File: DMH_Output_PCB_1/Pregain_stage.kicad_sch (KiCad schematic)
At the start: 9 parts, among them U7 TL072

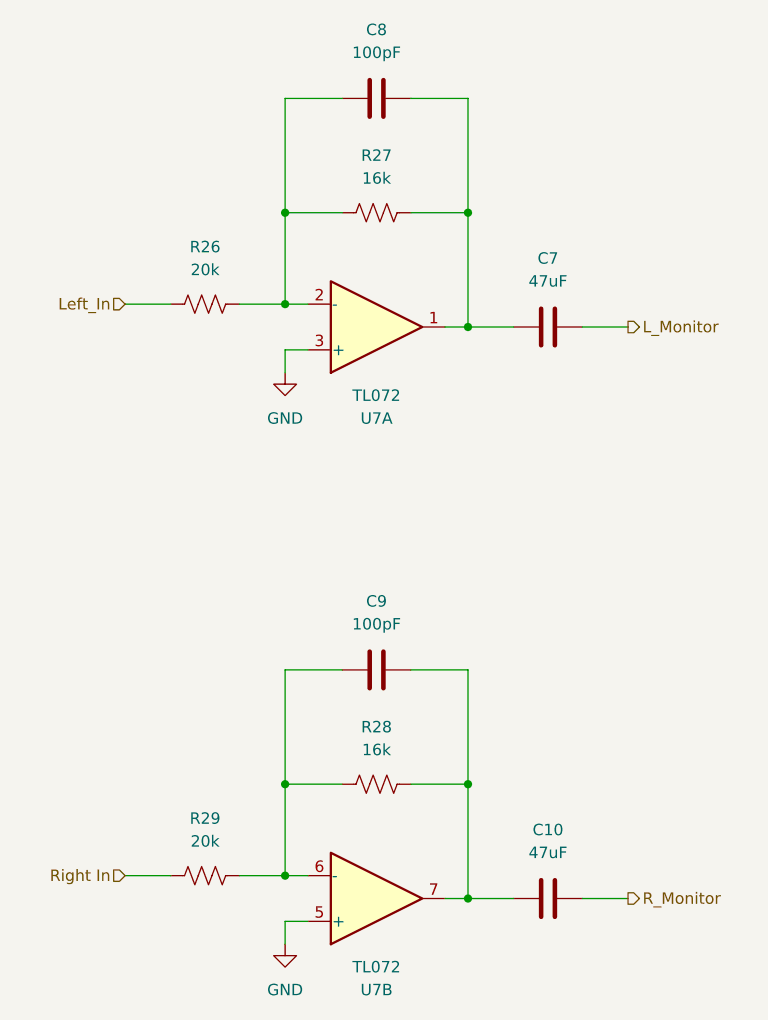
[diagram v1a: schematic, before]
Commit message: Redesigned external input preamp
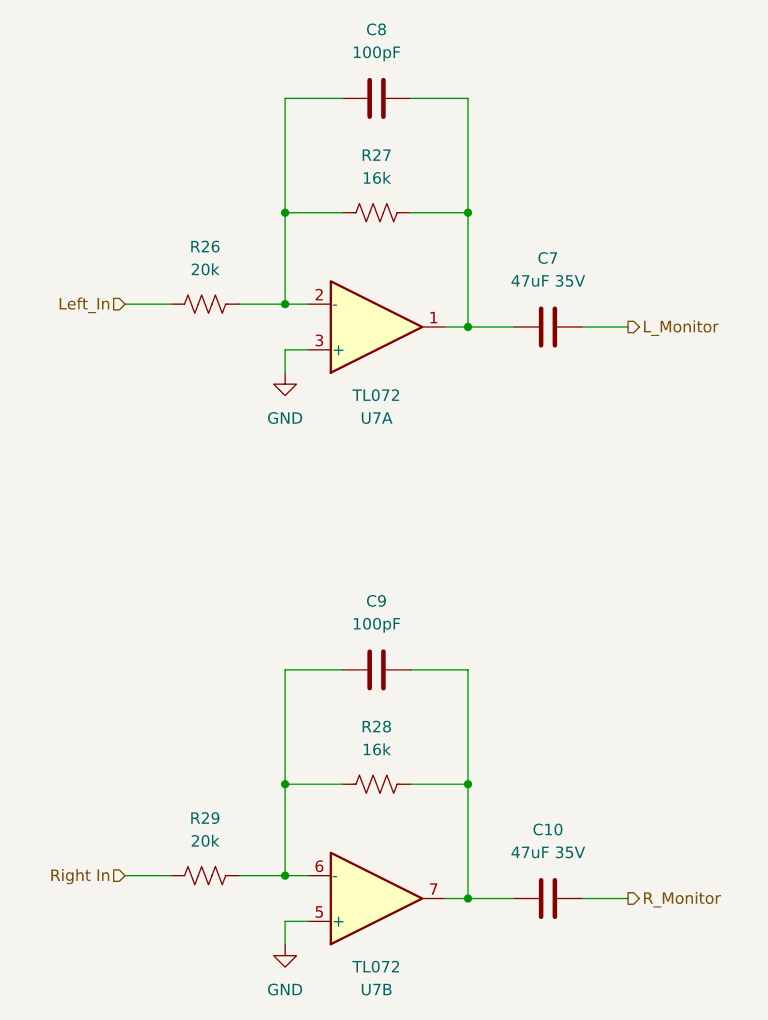
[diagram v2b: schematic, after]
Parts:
- C10, C7: value 47uF -> 47uF 35V; footprint Capacitor_THT:C_Disc_D4.3mm_W1.9mm_P5.00mm -> Capacitor_THT:C_Radial_D8.0mm_H11.5mm_P3.50mm
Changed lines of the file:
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@@
+	)
+	(symbol
+		(lib_id "Device:C")
+		(at 107.95 63.5 90)
+		(unit 1)
+		(exclude_from_sim no)
+		(in_bom yes)
+		(on_board yes)
+		(dnp no)
+		(fields_autoplaced yes)
+		(property "Reference" "C7"
+			(at 107.95 55.88 90)
+			(effects
+				(font
+					(size 1.27 1.27)
+				)
+			)
+		)
+		(property "Value" "47uF 35V"
+			(at 107.95 58.42 90)
+			(effects
+				(font
+					(size 1.27 1.27)
+				)
+			)
+		)
+		(property "Footprint" "Capacitor_THT:C_Radial_D8.0mm_H11.5mm_P3.50mm"
+			(at 111.76 62.5348 0)
+			(effects
+				(font
+					(size 1.27 1.27)
+				)
+				(hide yes)
+			)
+		)
+		(property "Datasheet" "~"
+			(at 107.95 63.5 0)
+			(effects
+				(font
+					(size 1.27 1.27)
+				)
+				(hide yes)
+			)
+		)
+		(property "Description" "Unpolarized capacitor"
+			(at 107.95 63.5 0)
+			(effects
+				(font
+					(size 1.27 1.27)
+				)
+				(hide yes)
+			)
+		)
+		(property "Function" ""
+			(at 107.95 63.5 0)
+			(effects
+				(font
+					(size 1.27 1.27)
+				)
+			)
+		)
+		(pin "1"
+		)
+		(pin "2"
+		)
+		(instances
+			(project "DMH_Output_PCB_1"
+				(path "/58f4306d-5387-4983-bb08-41a2313fd315/0b1658b3-ac7b-4692-8043-3e4b42d6c671"
+					(reference "C7")
+					(unit 1)
+				)
+			)
+		)
 	)
 	(symbol
@@
 	(symbol
 		(lib_id "Device:C")
-		(at 107.95 63.5 90)
-		(unit 1)
-		(exclude_from_sim no)
-		(in_bom yes)
-		(on_board yes)
-		(dnp no)
-		(fields_autoplaced yes)
-		(property "Reference" "C7"
-			(at 107.95 55.88 90)
-			(effects
-				(font
-					(size 1.27 1.27)
-				)
-			)
-		)
-		(property "Value" "47uF"
-			(at 107.95 58.42 90)
-			(effects
-				(font
-					(size 1.27 1.27)
-				)
-			)
-		)
-		(property "Footprint" "Capacitor_THT:C_Disc_D4.3mm_W1.9mm_P5.00mm"
-			(at 111.76 62.5348 0)
-			(effects
-				(font
-					(size 1.27 1.27)
-				)
-				(hide yes)
-			)
-		)
-		(property "Datasheet" "~"
-			(at 107.95 63.5 0)
-			(effects
-				(font
-					(size 1.27 1.27)
-				)
-				(hide yes)
-			)
-		)
-		(property "Description" "Unpolarized capacitor"
-			(at 107.95 63.5 0)
-			(effects
-				(font
-					(size 1.27 1.27)
-				)
-				(hide yes)
-			)
-		)
-		(pin "2"
-		)
-		(pin "1"
-		)
-		(instances
-			(project "DMH_Output_PCB_1"
-				(path "/58f4306d-5387-4983-bb08-41a2313fd315/0b1658b3-ac7b-4692-8043-3e4b42d6c671"
-					(reference "C7")
-					(unit 1)
-				)
-			)
-		)
-	)
-	(symbol
-		(lib_id "Device:C")
 		(at 107.95 127 90)
 		(unit 1)
@@
 			)
 		)
-		(property "Value" "47uF"
+		(property "Value" "47uF 35V"
 			(at 107.95 121.92 90)
 			(effects
@@
 			)
 		)
-		(property "Footprint" "Capacitor_THT:C_Disc_D4.3mm_W1.9mm_P5.00mm"
+		(property "Footprint" "Capacitor_THT:C_Radial_D8.0mm_H11.5mm_P3.50mm"
 			(at 111.76 126.0348 0)
 			(effects
@@
 			)
 		)
-		(pin "2"
-		)
-		(pin "1"
-		)
-		(instances
+		(property "Function" ""
+			(at 107.95 127 0)
+			(effects
+				(font
+					(size 1.27 1.27)
+				)
+			)
+		)
+		(pin "1"
+		)
+		(pin "2"
+		)
+		(instances

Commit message: Adjusted gains
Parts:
- R27, R28: value 16k -> 14k
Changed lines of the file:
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@@
 			)
 		)
-		(property "Value" "16k"
+		(property "Value" "14k"
 			(at 88.9 46.99 90)
 			(effects
@@
 				)
 				(hide yes)
+			)
+		)
+		(property "Function" ""
+			(at 88.9 50.8 0)
+			(effects
+				(font
+					(size 1.27 1.27)
+				)
 			)
 		)
@@
 			)
 		)
-		(property "Value" "16k"
+		(property "Value" "14k"
 			(at 88.9 110.49 90)
 			(effects
@@
 			)
 		)
+		(property "Function" ""
+			(at 88.9 114.3 0)
+			(effects
+				(font
+					(size 1.27 1.27)
+				)
+			)
+		)
